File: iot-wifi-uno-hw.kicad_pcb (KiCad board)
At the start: 2 copper layers, 64 x 52.8 mm, 59 parts, among them CON1 BARREL_JACK, P1 CONN_01X08, P2 CONN_01X08, P3 CONN_01X06, P4 CONN_01X10, P5 CONN_01X04, Q1 MMBT8050LT1G_BEC, Q2 MMBT8050LT1G_BEC, SW1 RST, SW2 GPIO0, U1 usb_mini_b, U2 AMS1117-5, U3 CH340G, U4 ESP-12E, U5 MCP6001R, U6 AMS1117-3.3, U7 IRLM6402, X1 CRYSTAL_ABM3C

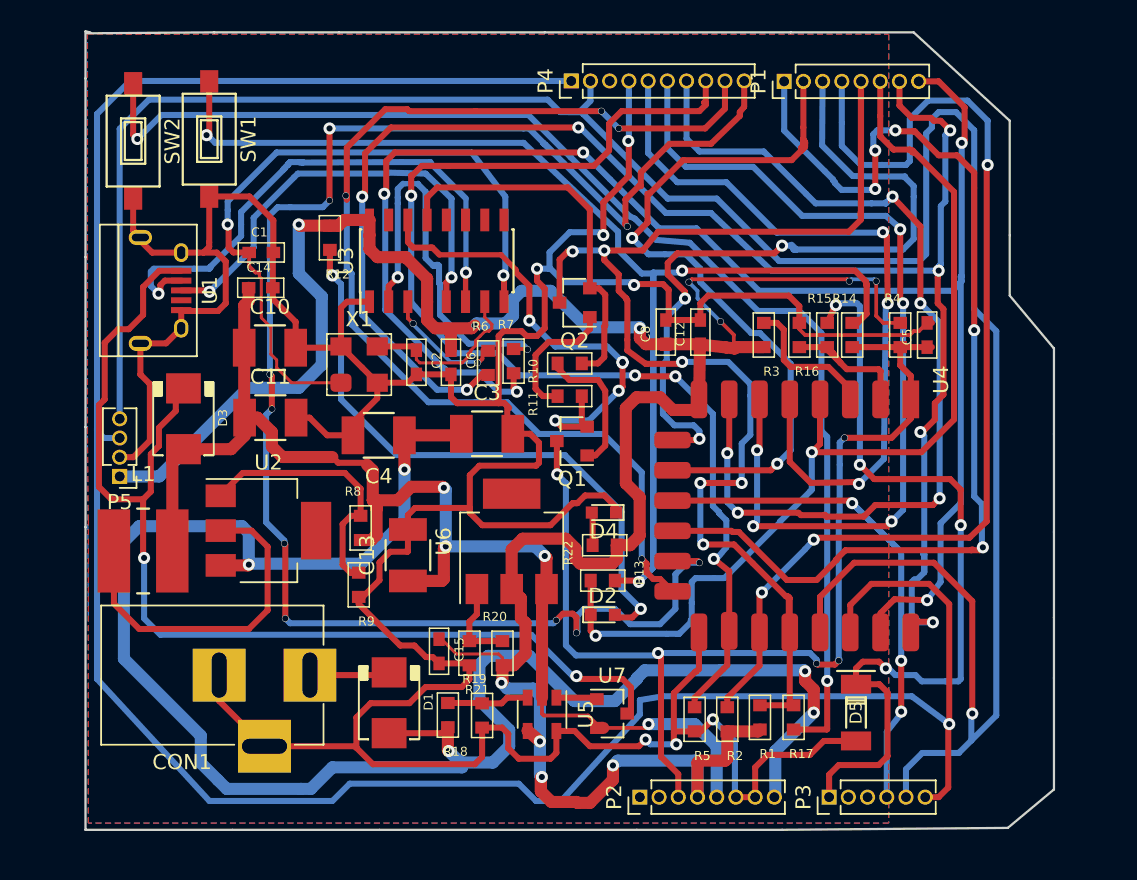
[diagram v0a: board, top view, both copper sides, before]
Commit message: PCB layout hoàn chỉnh, sửa khung, sửa 3d hoàn chỉnh
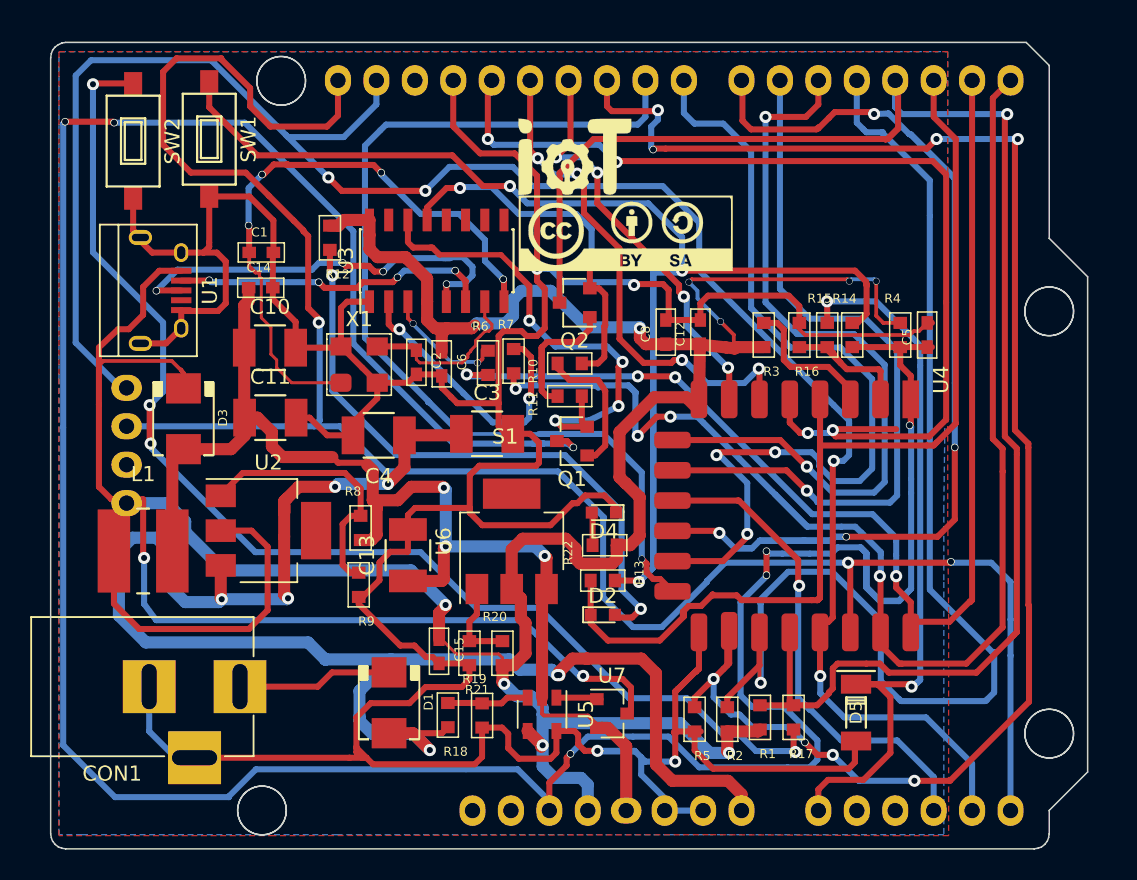
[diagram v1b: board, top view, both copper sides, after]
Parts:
- removed P1, P2: CONN_01X08, Pin_Headers:Pin_Header_Straight_1x08_Pitch1.27mm
- removed P3: CONN_01X06, Pin_Headers:Pin_Header_Straight_1x06_Pitch1.27mm
- removed P4: CONN_01X10, Pin_Headers:Pin_Header_Straight_1x10_Pitch1.27mm
- removed P5: CONN_01X04, Pin_Headers:Pin_Header_Straight_1x04_Pitch1.27mm
- added G***: LOGO, ESP8266:logo-iotmakervn_7.5x5, F.Cu at (239.0, 87.3)
- added G***: LOGO, ESP8266:logo_cc-bby-sa_14.1x5mm, F.Cu at (242.3, 92.3)
- added S1: ESP-UNO, ESP8266:shield-uno, F.Cu at (237.3, 107.6)
- U2: value AMS1117-5 -> AMS117-5.0
- moved CON1 4.69 mm to (216.8, 122.3)
- moved C6 0.62 mm to (230.2, 101.0)
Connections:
- U1 pad 4: Net-(U1-Pad4) -> (no net)
- U3 pad 10: Net-(U3-Pad10) -> (no net)
- U3 pad 11: Net-(U3-Pad11) -> (no net)
- U3 pad 12: Net-(U3-Pad12) -> (no net)
- U3 pad 15: Net-(U3-Pad15) -> (no net)
- U3 pad 9: Net-(U3-Pad9) -> (no net)
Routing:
- net REST: track 72.9 -> 207.5 mm, vias 5 -> 7
- net MOSI: track 109.8 -> 58.0 mm, vias 10 -> 3
- net GPIO4: track 165.1 -> 130.3 mm, vias 1 -> 4
- net GPIO13: track 62.5 -> 28.0 mm, vias 5 -> 4
- net GPIO15: track 77.3 -> 107.5 mm, vias 4 -> 8
- net TXD: track 108.5 -> 79.8 mm, vias 7 -> 4
- net GPIO12: track 59.1 -> 34.3 mm, vias 5 -> 4
- net GPIO5: track 159.1 -> 135.7 mm, vias 1 -> 3
- net GPIO2: track 70.2 -> 92.5 mm, vias 3 -> 1
- net GND: track 266.5 -> 286.9 mm, vias 7 -> 4
- net GPIO14: track 48.9 -> 68.1 mm, vias 3 -> 4
- net GPIO0: track 90.8 -> 108.5 mm, vias 6 -> 1
- net D-: track 38.3 -> 21.1 mm, vias 2 -> 4
- net RXD: track 106.2 -> 90.3 mm, vias 5 -> 4
- net Net-(R7-Pad2): track 30.4 -> 20.6 mm
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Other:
- board size 64 x 52.8 mm -> 68.5 x 53.3 mm
- net class Default: trace_width 0.25 -> 0.4

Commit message: pcb layout hoàn chỉnh, sửa lỗi vị trí linh kiện, schematic
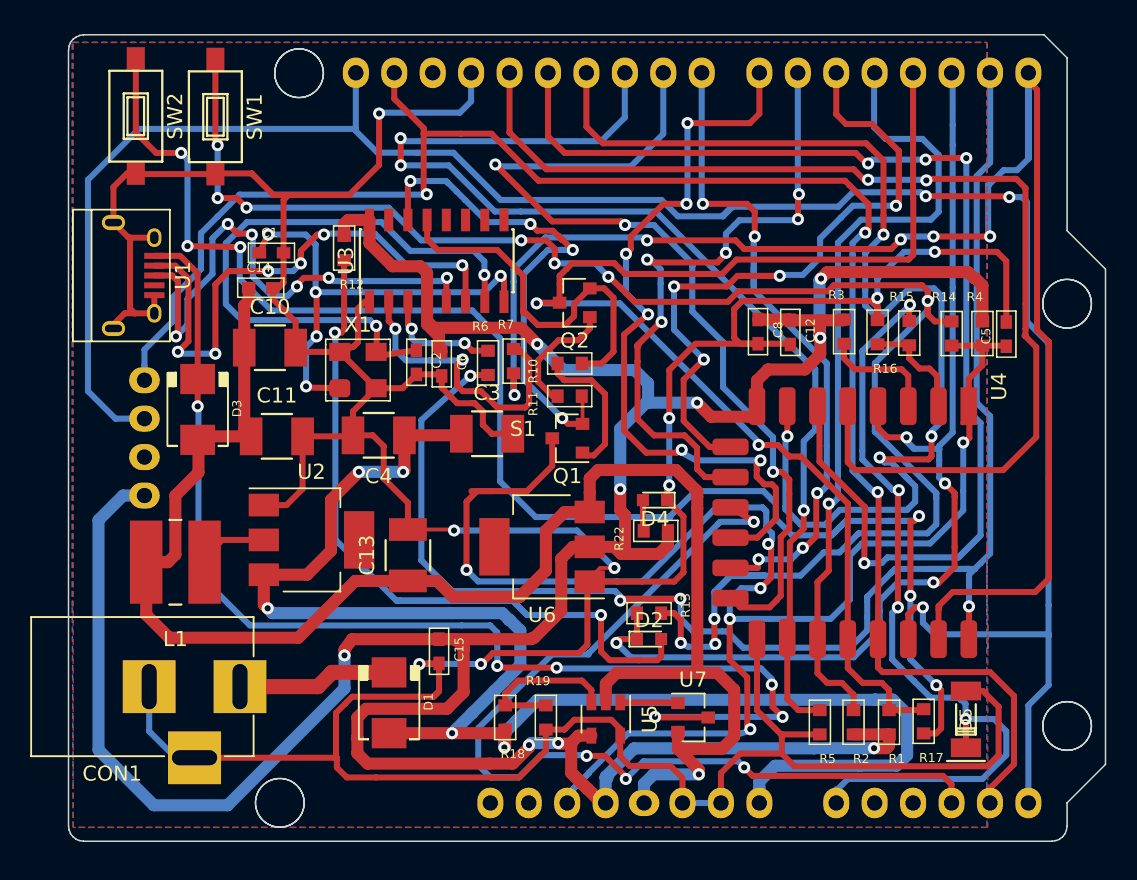
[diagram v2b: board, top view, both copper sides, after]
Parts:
- removed G***: LOGO, ESP8266:logo-iotmakervn_7.5x5
- removed G***: LOGO, ESP8266:logo_cc-bby-sa_14.1x5mm
- removed R20: 3K/1%, ESP8266:R_0603
- removed R21: 1K/1%, ESP8266:R_0603
- removed R8: 52.5K, ESP8266:R_0603
- removed R9: 10k, ESP8266:R_0603
- moved R17 8.60 mm to (262.0, 124.6)
- moved R1 8.54 mm to (259.7, 124.7)
- moved R2 8.35 mm to (257.4, 124.7)
- moved R5 8.28 mm to (255.2, 124.7)
- moved D5 7.28 mm to (264.8, 124.5), turned to 90 degrees
- moved R14 6.58 mm to (263.9, 99.0)
- moved C8 6.10 mm to (251.1, 98.8), turned to 270 degrees
- moved C12 5.94 mm to (253.2, 98.9), turned to 270 degrees
- moved R4 5.44 mm to (265.9, 99.0)
- moved R15 5.42 mm to (261.1, 98.9)
- moved U7 5.36 mm to (246.8, 124.3)
- moved R3 5.31 mm to (256.8, 98.8), turned to 90 degrees
- moved C5 5.23 mm to (267.5, 99.0)
- moved R16 5.17 mm to (259.0, 98.9)
- moved U5 4.23 mm to (241.0, 124.4)
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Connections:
- S1 pad 1: Net-(S1-Pad1) -> (no net)
- S1 pad 10: Net-(S1-Pad10) -> (no net)
- S1 pad 11: Net-(S1-Pad11) -> (no net)
- S1 pad 2: Net-(S1-Pad2) -> (no net)
- S1 pad 30: Net-(S1-Pad30) -> (no net)
- U1 pad 4: (no net) -> Net-(U1-Pad4)
- U2 pad 1: Net-(R8-Pad2) -> GND
- U3 pad 10: (no net) -> Net-(U3-Pad10)
- U3 pad 11: (no net) -> Net-(U3-Pad11)
- U3 pad 12: (no net) -> Net-(U3-Pad12)
- U3 pad 15: (no net) -> Net-(U3-Pad15)
- U3 pad 9: (no net) -> Net-(U3-Pad9)
- U6 pad 1: Net-(R20-Pad2) -> GND
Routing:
- net REST: track 207.5 -> 106.8 mm, vias 7 -> 6
- net +3V3: track 165.1 -> 217.0 mm, vias 10 -> 9
- net GPIO13: track 28.0 -> 77.4 mm
- net GPIO12: track 34.3 -> 79.5 mm
- net GPIO5: track 135.7 -> 178.2 mm
- net GPIO2: track 92.5 -> 53.1 mm
- net GPIO09: track 32.5 -> 63.5 mm, vias 1 -> 4
- net XI: track 11.7 -> 41.0 mm, vias 0 -> 2
- net GPIO15: track 107.5 -> 78.4 mm, vias 8 -> 3
- net TXD: track 79.8 -> 108.8 mm
- net +5V: track 85.7 -> 111.7 mm, vias 3 -> 1
- net GPIO0: track 108.5 -> 84.0 mm, vias 1 -> 2
- net GPIO10: track 73.0 -> 50.4 mm, vias 4 -> 6
- net Net-(R17-Pad2): track 81.5 -> 100.0 mm, vias 4 -> 6
- net Net-(L1-Pad1): track 22.6 -> 4.70 mm
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
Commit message: PCB layout sửa xong
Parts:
- removed C10, C11: 10uF/25V, ESP8266:C_1210
- removed D1: SS24, ESP8266:do214aa-g
- removed L1: 22uH, Choke_SMD:Choke_SMD_Wuerth-WE-PD2-Typ-MS
- added G***: LOGO, ESP8266:GPIO0, F.Cu at (210.7, 84.8)
- added G***: LOGO, ESP8266:logo-jack-5528, F.Cu at (209.6, 131.4)
- added G***: LOGO, ESP8266:GPIO16, F.Cu at (247.1, 119.4)
- added G***: LOGO, ESP8266:LEDPWR, F.Cu at (246.7, 111.5)
- added G***: LOGO, ESP8266:RST, F.Cu at (217.3, 84.8)
- added G***: LOGO, ESP8266:logo-jack_7.4x3, F.Cu at (209.4, 129.2)
- added G***: LOGO, ESP8266:logo_cc-bby-sa_14.1x5mm, F.Cu at (248.3, 94.0)
- added G***: LOGO, ESP8266:logo-iotmakervn_7, F.Cu at (207.3, 106.7)
- added G***: LOGO, ESP8266:logo-iotmakervn_7.5x5, F.Cu at (245.0, 88.4)
- added G***: LOGO, ESP8266:logo_openhardware_5x5mm, F.Cu at (262.1, 87.9)
- C3, C4: value 10uF/50V -> 1uF/25V
- moved U2 3.81 mm to (217.8, 112.6)
- moved C13 2.63 mm to (225.3, 113.6)
- moved SW2 2.50 mm to (207.5, 85.0)
- moved D3 2.44 mm to (216.4, 104.5)
- moved SW1 1.40 mm to (213.8, 84.9)
- moved U5 0.84 mm to (241.0, 123.6)
- moved R18 0.44 mm to (234.5, 124.8)
- moved R19 0.39 mm to (237.3, 124.7)
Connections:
- C4 pad 1: Vin -> +5V
- CON1 pad 1: Net-(CON1-Pad1) -> Vin
- U2 pad 2: Net-(L1-Pad1) -> +5V
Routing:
- net +3V3: track 217.0 -> 256.8 mm, vias 9 -> 7
- net Vin: track 102.1 -> 131.3 mm, vias 5 -> 7
- net GND: track 302.8 -> 326.9 mm, vias 9 -> 11
- net Net-(CON1-Pad1): track 22.4 -> 0.00 mm
- net D-: track 37.1 -> 50.4 mm, vias 6 -> 4
- net +5V: track 111.7 -> 122.7 mm
- net GPIO09: track 63.5 -> 54.9 mm
- net Net-(R18-Pad1): track 10.6 -> 18.4 mm, vias 0 -> 2
- net Net-(L1-Pad1): track 4.70 -> 0.00 mm
- net TXD: track 108.8 -> 106.2 mm
- net REST: track 106.8 -> 105.4 mm
- net Net-(D2-Pad2): track 56.2 -> 54.8 mm
- net VCC: track 82.2 -> 83.3 mm, vias 6 -> 4
- net XO: track 31.2 -> 30.3 mm
- net Net-(U5-Pad1): track 3.84 -> 4.57 mm
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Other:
- net class Default: via_dia 0.8 -> 1
- net class Power: trace_width 0.8 -> 1; via_dia 0.8 -> 1

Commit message: pcb hoàn chỉnh, sửa lỗi 3d, schematic, tên footprint
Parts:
- removed the G*** at (247.1, 119.4)
- removed the G*** at (246.7, 111.5)
- added D1: SCHOTTKY, ESP8266:do214aa-g, F.Cu at (216.5, 112.6)
- moved R12 29.9 mm to (253.1, 98.8)
- moved C14 29.7 mm to (237.2, 118.8), turned to 180 degrees
- moved G*** 24.1 mm to (220.9, 90.6)
- moved C12 17.1 mm to (238.8, 108.0), turned to 0 degrees
- moved C3 13.9 mm to (221.2, 112.6), turned to 270 degrees
- moved U2 11.9 mm to (225.4, 121.7), turned to 180 degrees
- moved U3 10.8 mm to (230.2, 104.9)
- moved C15 7.22 mm to (237.2, 120.9), turned to 180 degrees
- moved C4 6.98 mm to (225.5, 112.7), turned to 270 degrees
- moved G*** 6.64 mm to (241.9, 92.3)
- moved C1 5.98 mm to (222.0, 98.8), turned to 90 degrees
- moved R13 4.99 mm to (244.8, 112.5)
- moved D2 4.89 mm to (244.7, 114.3)
- moved C13 4.26 mm to (229.5, 112.6), turned to 270 degrees
- moved G*** 2.66 mm to (261.9, 90.6)
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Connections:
- CON1 pad 1: Vin -> Net-(CON1-Pad1)
- S1 pad 1: (no net) -> Net-(S1-Pad1)
- S1 pad 10: (no net) -> Net-(S1-Pad10)
- S1 pad 11: (no net) -> Net-(S1-Pad11)
- S1 pad 2: (no net) -> Net-(S1-Pad2)
- S1 pad 30: (no net) -> Net-(S1-Pad30)
- S1 pad 35: (no net) -> GND
- U1 pad 4: Net-(U1-Pad4) -> (no net)
- U3 pad 10: Net-(U3-Pad10) -> (no net)
- U3 pad 11: Net-(U3-Pad11) -> (no net)
- U3 pad 12: Net-(U3-Pad12) -> (no net)
- U3 pad 15: Net-(U3-Pad15) -> (no net)
- U3 pad 9: Net-(U3-Pad9) -> (no net)
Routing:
- net +3V3: track 256.8 -> 218.6 mm, vias 7 -> 8
- net Net-(R6-Pad2): track 7.91 -> 39.8 mm
- net Vin: track 131.3 -> 104.3 mm, vias 7 -> 5
- net Net-(R7-Pad2): track 19.7 -> 43.3 mm
- net Net-(Q1-Pad2): track 34.7 -> 14.8 mm, vias 4 -> 0
- net D-: track 50.4 -> 33.3 mm, vias 4 -> 2
- net Net-(D2-Pad2): track 54.8 -> 38.1 mm
- net Net-(CON1-Pad1): track 0.00 -> 15.6 mm
- net Net-(R18-Pad1): track 18.4 -> 3.81 mm, vias 2 -> 0
- net Net-(Q2-Pad2): track 35.0 -> 21.3 mm, vias 0 -> 2
- net XI: track 41.3 -> 29.6 mm
- net Net-(R13-Pad2): track 114.5 -> 103.9 mm, vias 10 -> 6
- net TXD: track 106.2 -> 96.7 mm
- net +5V: track 122.7 -> 131.0 mm, vias 1 -> 5
- net XO: track 30.3 -> 23.3 mm, vias 5 -> 2
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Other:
- board text added: "3,3V"
- board text added: "3.3V"
- board text added: "5V"
- board text added: "ADC"
- board text added: "CK/GPIO06"
- board text added: "CS/GPIO11"
- board text added: "GND"
- board text added: "GPIO0"
- board text added: "GPIO02"
- board text added: "GPIO04"
- board text added: "GPIO05"
- board text added: "GPIO09"
- board text added: "GPIO10"
- board text added: "GPIO12"
- board text added: "GPIO13"
- board text added: "GPIO14"
- board text added: "GPIO15"
- board text added: "GPIO16"
- board text added: "RST"
- board text added: "RXD/GPIO03"
- board text added: "SCL/GPIO5"
- board text added: "SDA/GPIO4"
- board text added: "SI/GPIO08"
- board text added: "SO/GPIO07"
- board text added: "TXD/GPIO01"
- board text added: "VIN"
- board text added: "https://arduino.esp8266.vn"
- board text added: "maker.vn"
